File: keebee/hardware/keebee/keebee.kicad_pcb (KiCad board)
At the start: 2 copper layers, 152 parts, among them J1 USB_B_Micro, SW1 SW_SPST, SW10 SW_SPST, SW11 SW_SPST, SW12 SW_SPST, SW13 SW_SPST, SW14 SW_SPST, SW15 SW_SPST, SW16 SW_SPST, SW17 SW_SPST, SW18 SW_SPST, SW19 SW_SPST, SW2 SW_SPST, SW20 SW_SPST, SW21 SW_SPST, SW22 SW_SPST, SW23 SW_SPST, SW24 SW_SPST, SW25 SW_SPST, SW26 SW_SPST, SW27 SW_SPST, SW28 SW_SPST, SW29 SW_SPST, SW3 SW_SPST, SW30 SW_SPST, SW31 SW_SPST, SW32 SW_SPST, SW33 SW_SPST, SW34 SW_SPST, SW35 SW_SPST, SW36 SW_SPST, SW37 SW_SPST, SW38 SW_SPST, SW39 SW_SPST, SW4 SW_SPST, SW40 SW_RST, SW41 SW_SPST, SW42 SW_SPST, SW43 SW_SPST, SW44 SW_SPST, SW45 SW_SPST, SW46 SW_SPST, SW47 SW_SPST, SW48 SW_SPST, SW49 SW_SPST, SW5 SW_SPST, SW50 SW_SPST, SW51 SW_SPST, SW52 SW_SPST, SW53 SW_SPST, SW54 SW_SPST, SW55 SW_SPST, SW56 SW_SPST, SW57 SW_SPST, SW58 SW_SPST, SW59 SW_SPST, SW6 SW_SPST, SW60 SW_SPST, SW61 SW_SPST, SW62 SW_SPST, SW63 SW_SPST, SW64 SW_SPST, SW65 SW_SPST, SW66 SW_SPST, SW67 SW_SPST, SW68 SW_SPST, SW69 SW_SPST, SW7 SW_SPST, SW70 SW_SPST, SW8 SW_SPST, SW9 SW_SPST, U1 LM1117-3.3

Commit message: Fixup imported footprint errors.
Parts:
- removed R3: 10K, Resistors_SMD:R_0805_HandSoldering
- added J2: Conn_ARM_JTAG_SWD_10, Pin_Headers:Pin_Header_Straight_2x05_Pitch1.27mm_SMD, F.Cu at (61.5, 171.3)
- added U2: STM32F042K6Tx, Housings_QFP:LQFP-32_7x7mm_Pitch0.8mm, F.Cu at (47.5, 165.5)
- moved SW19 156.6 mm to (146.9, 142.6)
- moved SW25 156.6 mm to (127.7, 142.6)
- moved SW33 156.6 mm to (108.5, 142.6)
- moved SW36 155.9 mm to (185.3, 46.6)
- moved SW20 145.5 mm to (261.9, 27.4)
- moved SW21 117.0 mm to (185.3, 142.6)
- moved SW28 101.7 mm to (185.3, 65.8)
- moved SW13 99.6 mm to (146.9, 85.0)
- moved SW5 84.4 mm to (166.1, 65.8)
- moved SW6 78.5 mm to (166.1, 142.6)
- moved D66 76.3 mm to (271.4, 24.0)
- moved SW22 75.9 mm to (108.5, 85.0)
- moved SW37 72.1 mm to (70.1, 142.6)
- moved D8 67.3 mm to (266.6, 62.4)
- moved D65 62.2 mm to (233.1, 81.6)
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
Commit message: Initial PCB outline.
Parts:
- moved D16 179.2 mm to (304.5, 257.4)
- moved D24 179.2 mm to (309.3, 257.4)
- moved D44 179.2 mm to (299.8, 257.4)
- moved R2 179.2 mm to (126.2, 342.4)
- moved C1 179.2 mm to (134.7, 336.3)
- moved C2 179.2 mm to (134.7, 338.1)
- moved C3 179.2 mm to (130.8, 344.2)
- moved C4 179.2 mm to (134.7, 339.9)
- moved D11 179.2 mm to (304.5, 262.1)
- moved D12 179.2 mm to (299.8, 262.1)
- moved D13 179.2 mm to (304.5, 259.8)
- moved D14 179.2 mm to (299.8, 259.8)
- moved D15 179.2 mm to (299.8, 252.7)
- moved D18 179.2 mm to (309.3, 255.1)
- moved D19 179.2 mm to (304.5, 255.1)
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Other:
- board outline added: 275 x 103 mm

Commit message: Place all switches.
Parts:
- moved SW6 327.9 mm to (62.0, 29.0)
- moved SW21 309.9 mm to (119.0, 29.0)
- moved SW11 307.4 mm to (81.0, 29.0)
- moved SW8 304.0 mm to (62.0, 67.0)
- moved SW12 296.1 mm to (81.1, 48.0)
- moved SW51 290.4 mm to (233.0, 29.0)
- moved SW9 287.5 mm to (62.0, 86.0)
- moved SW16 280.6 mm to (100.0, 29.0)
- moved SW7 278.7 mm to (62.0, 48.0)
- moved SW10 271.2 mm to (62.0, 105.0)
- moved SW17 269.5 mm to (100.0, 48.0)
- moved SW37 263.9 mm to (176.0, 48.0)
- moved SW14 261.4 mm to (81.0, 86.0)
- moved SW18 259.3 mm to (100.0, 67.0)
- moved SW68 252.4 mm to (290.0, 67.0)
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
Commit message: Place key diodes.
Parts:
- moved D2 360.8 mm to (29.2, 28.8), turned to 90 degrees
- moved D7 347.0 mm to (49.8, 29.2), turned to 90 degrees
- moved D3 341.1 mm to (29.2, 48.0), turned to 90 degrees
- moved D8 336.1 mm to (49.8, 48.3), turned to 90 degrees
- moved D4 334.2 mm to (29.2, 67.3), turned to 90 degrees
- moved D5 328.2 mm to (29.2, 86.4), turned to 90 degrees
- moved D12 328.0 mm to (68.8, 29.2), turned to 90 degrees
- moved D6 322.8 mm to (29.2, 105.8), turned to 90 degrees
- moved D9 319.8 mm to (49.8, 67.3), turned to 90 degrees
- moved D13 316.7 mm to (68.8, 48.3), turned to 90 degrees
- moved D17 309.2 mm to (87.9, 29.2), turned to 90 degrees
- moved D10 307.0 mm to (49.8, 86.2), turned to 90 degrees
- moved D18 303.0 mm to (87.9, 48.1), turned to 90 degrees
- moved D22 301.5 mm to (106.9, 29.2), turned to 90 degrees
- moved D14 300.6 mm to (68.8, 67.3), turned to 90 degrees
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
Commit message: Roughly place all footprints.
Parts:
- removed SW40: SW_RST, Buttons_Switches_THT:SW_TH_Tactile_Omron_B3F-10xx
- added SW_RST: SW_RST, Buttons_Switches_THT:SW_TH_Tactile_Omron_B3F-10xx, B.Cu at (140.3, 63.2)
- C1, C2, C3, C4, J2, SW_BOOT0, SW_LAYOUT1, U1, U2: moved to B.Cu
- moved J1 324.3 mm to (69.1, 20.8), turned to 180 degrees
- moved U1 297.0 mm to (68.8, 38.5), turned to 270 degrees
- moved SW_BOOT0 279.3 mm to (164.1, 63.0)
- moved J2 278.8 mm to (158.2, 60.5), turned to 270 degrees
- moved SW_LAYOUT1 274.6 mm to (151.1, 60.7)
- moved C1 236.8 mm to (159.5, 100.8), turned to 180 degrees
- moved C3 233.9 mm to (159.3, 112.0), turned to 270 degrees
- moved D1 225.0 mm to (149.0, 118.1), turned to 180 degrees
- moved C2 224.9 mm to (145.8, 113.5)
- moved C4 224.4 mm to (145.8, 115.8)
- moved R2 222.4 mm to (149.0, 121.2), turned to 180 degrees
- moved R1 217.9 mm to (179.2, 121.2)
- moved D41 215.4 mm to (179.2, 118.1)
- moved U2 35.5 mm to (152.4, 107.4), turned to 180 degrees

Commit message: Route rows and columns from scan matrix.
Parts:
- moved U1 19.1 mm to (49.8, 40.1)
- moved J1 19.1 mm to (50.0, 21.1)
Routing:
- net /ROW3: track 0.00 -> 247.1 mm
- net /ROW2: track 0.00 -> 247.0 mm
- net /ROW1: track 0.00 -> 247.0 mm
- net /ROW4: track 0.00 -> 247.0 mm
- net /ROW0: track 0.00 -> 247.0 mm
- net /COL13: track 0.00 -> 81.9 mm, vias 0 -> 8
- net /COL9: track 0.00 -> 81.9 mm, vias 0 -> 8
- net /COL2: track 0.00 -> 81.9 mm, vias 0 -> 8
- net /COL3: track 0.00 -> 81.9 mm, vias 0 -> 8
- net /COL10: track 0.00 -> 81.8 mm, vias 0 -> 8
- net /COL12: track 0.00 -> 81.8 mm, vias 0 -> 8
- net /COL11: track 0.00 -> 81.8 mm, vias 0 -> 8
- net /COL5: track 0.00 -> 81.7 mm, vias 0 -> 8
- net /COL6: track 0.00 -> 81.7 mm, vias 0 -> 8
- net /COL0: track 0.00 -> 80.0 mm
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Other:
- rule trace_min: 0.2 -> 0.1524
- rule via_min_drill: 0.3 -> 0.3302
- rule via_min_size: 0.4 -> 0.6858

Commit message: Route more trackes.
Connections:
- D42 pad 1: Net-(D42-Pad1) -> /COL8
- D43 pad 1: Net-(D42-Pad1) -> /COL8
- D44 pad 1: Net-(D42-Pad1) -> /COL8
- D45 pad 1: Net-(D42-Pad1) -> /COL8
- D46 pad 1: Net-(D42-Pad1) -> /COL8
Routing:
- net /COL0: track 80.0 -> 220.5 mm, vias 0 -> 1
- net /COL1: track 61.4 -> 180.2 mm, vias 6 -> 7
- net /COL8: track 0.00 -> 98.9 mm, vias 0 -> 7
- net /COL2: track 81.9 -> 177.5 mm, vias 8 -> 9
- net /COL3: track 81.9 -> 155.4 mm, vias 8 -> 9
- net Net-(D42-Pad1): track 61.3 -> 0.00 mm, vias 6 -> 0
- net /COL9: track 81.9 -> 138.8 mm, vias 8 -> 9
- net /COL4: track 61.4 -> 114.1 mm, vias 6 -> 7
- net /COL7: track 61.5 -> 93.8 mm, vias 6 -> 7
- net /COL5: track 81.7 -> 113.5 mm, vias 8 -> 9
- net /COL6: track 81.7 -> 93.9 mm, vias 8 -> 9

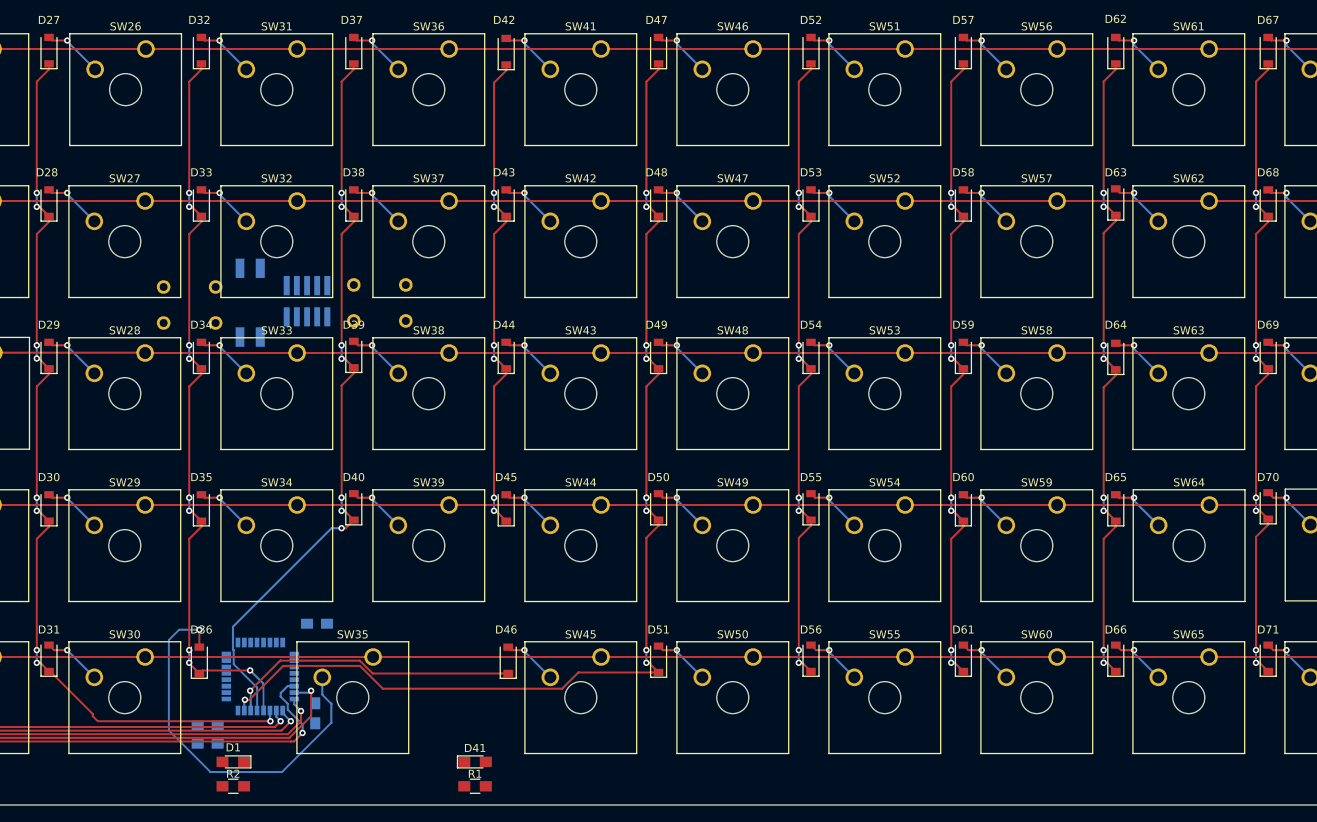
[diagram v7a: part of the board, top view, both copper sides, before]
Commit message: Route some more MCU pins.
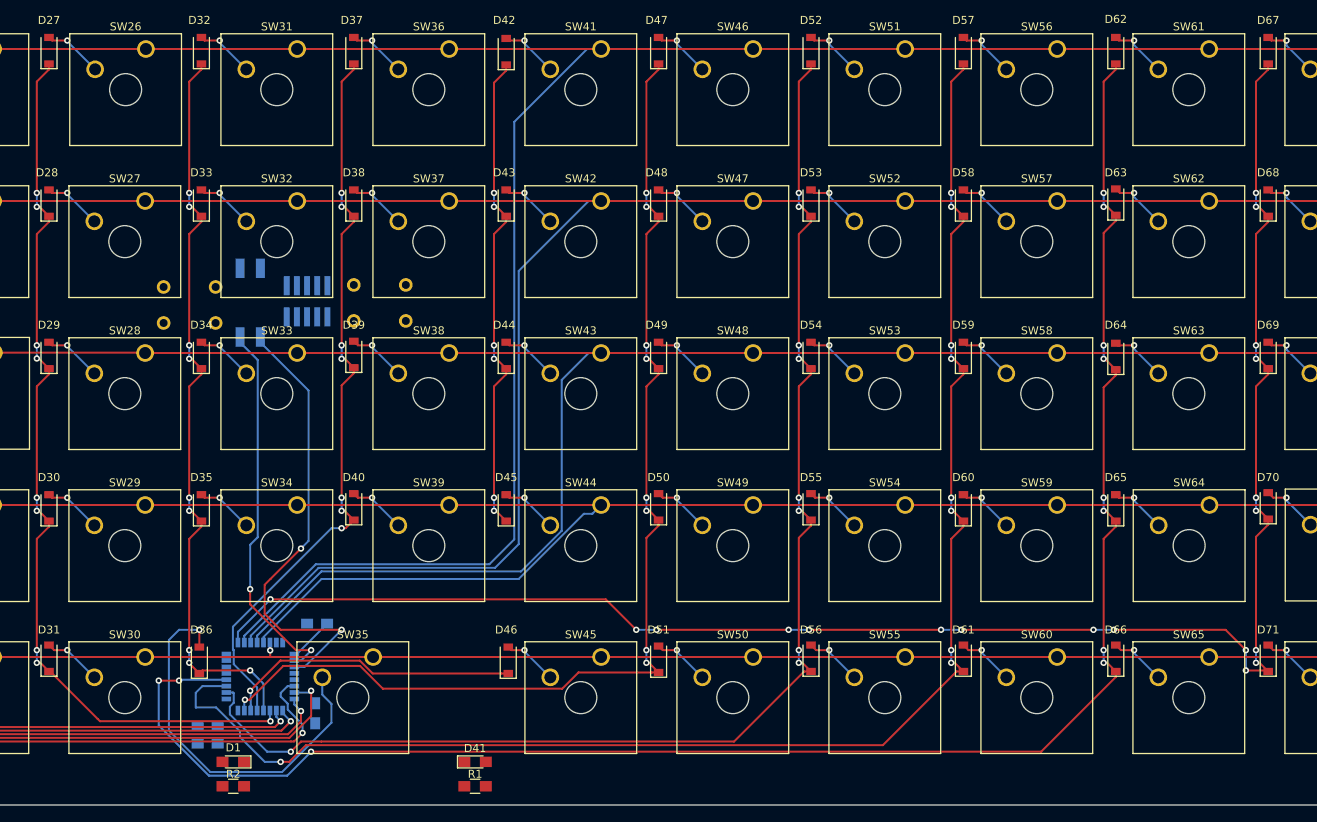
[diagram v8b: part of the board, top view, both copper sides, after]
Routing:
- net /COL12: track 81.8 -> 223.9 mm, vias 8 -> 11
- net /COL13: track 81.9 -> 218.9 mm, vias 8 -> 19
- net /COL11: track 81.8 -> 191.6 mm, vias 8 -> 9
- net /ROW0: track 247.0 -> 355.1 mm
- net /ROW1: track 247.0 -> 334.2 mm
- net /COL10: track 81.8 -> 164.4 mm, vias 8 -> 9
- net /ROW2: track 247.0 -> 316.6 mm
- net Net-(SW_LAYOUT1-Pad3): track 0.00 -> 57.6 mm, vias 0 -> 2
- net /ROW3: track 247.1 -> 296.8 mm
- net Net-(SW_LAYOUT1-Pad4): track 0.00 -> 47.4 mm, vias 0 -> 2
- net +3V3: track 0.00 -> 5.67 mm
- net /ROW4: track 247.0 -> 248.8 mm, vias 0 -> 1
